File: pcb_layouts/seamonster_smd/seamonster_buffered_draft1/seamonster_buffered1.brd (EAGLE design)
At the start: 172.5 x 106.5 mm, 84 parts, among them IC1 7805T, IC2 4051D, IC3 4051D, IC4 DG408DY, IC5 4040D, IC6 40106D, IC7 4070D, Q1 THONKICONNNEW, Q2 THONKICONNNEW, Q3 THONKICONNNEW, Q4 THONKICONNNEW, Q5 THONKICONNNEW, Q6 THONKICONNNEW, SW1 T-80-T-SPDT-ON-OFF-ON, SW2 T-80-T-SPDT-ON-OFF-ON, SW3 T-80-T-SPDT-ON-OFF-ON, SW4 T-80-T-SPDT-ON-OFF-ON

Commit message: figured out invoking across multiple sheets
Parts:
- removed IC5: 4040D, 40xx:SO16
- removed LED10, LED11, LED12, LED13, LED14, LED9: (no value), SparkFun-LED:LED3MM
- removed Q1, Q2, Q3, Q4, Q5, Q6: THONKICONNNEW, MusicThingModular:WQP-PJ301M-12_JACK
- removed R10, R11, R12, R13, R14, R9: (no value), SparkFun-Resistors:0805
- added U1: TL084, MusicThingModular:SO14
- moved C5 521.2 mm to (-403.9, -256.5)
- moved C6 521.2 mm to (-407.7, -256.5)
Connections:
- removed net N$34: LED9.A, R9.1
- removed net N$35: LED10.A, R10.1
- removed net N$36: LED11.A, R11.1
- removed net N$37: LED12.A, R12.1
- removed net N$38: LED13.A, R13.1
- removed net N$39: LED14.A, R14.1
- removed net N$40: IC5.9, Q1.P$1_TIP, R9.2
- removed net N$41: IC5.7, Q2.P$1_TIP, R10.2
- removed net N$42: IC5.6, Q3.P$1_TIP
- removed net N$43: IC5.5, Q4.P$1_TIP
- removed net N$44: IC5.3, Q5.P$1_TIP
- removed net N$45: IC5.2, Q6.P$1_TIP
- removed net N$48: R11.2
- removed net N$49: R12.2
- removed net N$50: R13.2
- removed net N$51: R14.2
- new net CCO1_BUFFERED: U1.1, U1.2
- new net CCO2_BUFFERED: U1.6, U1.7
- new net CCO3_BUFFERED: U1.8, U1.9
- new net CCO4_BUFFERED: U1.13, U1.14
- new net VEE: IC2.7, IC3.7
- net CCO1: now also U1.3
- net GND: no longer IC2.7, IC3.7, LED10.K, LED11.K, LED12.K, LED13.K, LED14.K, LED9.K, Q1.P$3_SLEEVE, Q2.P$3_SLEEVE, Q3.P$3_SLEEVE, Q4.P$3_SLEEVE, Q5.P$3_SLEEVE, Q6.P$3_SLEEVE
- net N$54: now also U1.5
- net N$57: now also U1.10
- net N$61: now also U1.12
- net V+: now also C5.1, U1.4
- net V-: now also C6.1, U1.11
- net VCC: no longer C5.1, C6.1
- net VDD: no longer IC5.16
- net VSS: no longer IC5.8

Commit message: fleshed out schematic pages
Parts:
- added C15, C16, C17, C18, C19, C20: 0.1µF, SparkFun-Capacitors:0805
- added IC5, IC8: 4046D, 40xx:SO16
- added U2: TL084, MusicThingModular:SO14
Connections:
- removed net VEE: IC2.7, IC3.7
- new net COMPLEX_OUT1_BUFFERED: U2.1, U2.2
- new net COMPLEX_OUT2_BUFFERED: U2.6, U2.7
- new net N$34: IC7.1
- new net N$35: IC7.3, IC7.5
- new net N$36: IC7.10, IC7.12
- new net N$37: IC7.8
- new net N$38: IC7.4, U2.3
- new net N$39: IC7.11, U2.5
- net CCO1_BUFFERED: now also IC7.2
- net CCO2_BUFFERED: now also IC7.6
- net CCO3_BUFFERED: now also IC7.9
- net CCO4_BUFFERED: now also IC7.13
- net GND: now also C15.2, C16.2, C17.2, C18.2, C19.2, C20.2, IC2.7, IC3.7, IC6.7, IC7.7
- net V+: now also C18.1, U2.4
- net V-: now also C19.1, U2.11
- net VCC: now also C15.1, C16.1, C17.1, C20.1, IC6.14, IC7.14
- net VDD: now also IC5.16, IC8.16; no longer IC6.14, IC7.14
- net VSS: now also IC5.8, IC8.8; no longer IC6.7, IC7.7

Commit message: added in VCOs and more buffering
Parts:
- added C21, C22, C25, C26, C27, C28, C29: 0.1µF, SparkFun-Capacitors:0805
- added C23, C24: 1µF, SparkFun-Capacitors:0805
- added CLOCK_IN, CV_OUT, Q1, Q2, Q3, Q4, Q5, Q6: THONKICONNNEW, MusicThingModular:WQP-PJ301M-12_JACK
- added CLOCK_SELECT: T-80-T-SPDT-ON-OFF-ON, MusicThingModular:M9040P
- added IC9: 4040D, 40xx:SO16
- added LED10, LED11, LED12, LED13, LED14, LED9: (no value), SparkFun-LED:LED3MM
- added R10, R11, R12, R13, R14, R15, R16, R17, R18, R9: (no value), SparkFun-Resistors:0805
- added U3: TL084, MusicThingModular:SO14
- added VR13, VR14: 1MΩ, MusicThingModular:9MM_SNAP-IN_POT
- added VR15: 100KΩ, MusicThingModular:9MM_SNAP-IN_POT
- VR1, VR10, VR11, VR12, VR2, VR3, VR4, VR5, VR6, VR7, VR8: value (none) -> 100KΩ
- moved VR8 923.1 mm to (-468.6, -584.2), turned to 0 degrees
- moved VR7 886.7 mm to (-468.6, -552.5), turned to 0 degrees
- moved VR6 850.4 mm to (-468.6, -520.7), turned to 0 degrees
- moved VR5 814.1 mm to (-468.6, -488.9), turned to 0 degrees
- moved VR4 777.9 mm to (-468.6, -457.2), turned to 0 degrees
- moved VR3 741.8 mm to (-468.6, -425.4), turned to 0 degrees
- moved VR2 705.9 mm to (-468.6, -393.7), turned to 0 degrees
- moved VR10 699.2 mm to (-664.2, -793.8)
- moved VR11 699.2 mm to (-664.2, -825.5)
- moved VR12 699.2 mm to (-664.2, -857.2)
- moved VR9 699.2 mm to (-664.2, -762.0)
- moved VR1 670.0 mm to (-468.6, -361.9), turned to 0 degrees
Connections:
- removed net VDD: IC5.16, IC8.16
- removed net VSS: IC5.8, IC8.8
- new net CV_OUT_BUFFERED: CV_OUT.P$1_TIP, IC5.9, IC8.9, U2.8, U2.9
- new net N$40: IC5.12, R15.2
- new net N$41: IC6.1, VR15.1
- new net N$42: R15.1, VR13.3
- new net N$43: CLOCK_SELECT.3, IC6.2, VR15.2
- new net N$44: C23.1, IC5.6
- new net N$45: C23.2, IC5.7
- new net N$48: C24.1, IC8.6
- new net N$49: C24.2, IC8.7
- new net N$50: CLOCK_SELECT.2, IC9.10
- new net N$51: LED9.A, R9.2
- new net N$65: LED10.A, R10.2
- new net N$66: LED11.A, R11.2
- new net N$67: LED12.A, R12.2
- new net N$68: LED13.A, R13.2
- new net N$69: LED14.A, R14.2
- new net N$70: CLOCK_IN.P$1_TIP, CLOCK_SELECT.1
- new net N$71: IC8.12, R16.2
- new net N$72: R16.1, VR14.3
- new net N$74: IC8.11, R18.2
- new net N$75: IC5.11, R17.2
- new net Q1: IC9.9, Q1.P$1_TIP, R9.1
- new net Q2: IC9.7, Q2.P$1_TIP, R10.1
- new net Q3: IC9.6, Q3.P$1_TIP, R11.1
- new net Q4: IC9.5, Q4.P$1_TIP, R12.1
- new net Q5: IC9.3, Q5.P$1_TIP, R13.1
- new net Q6: IC9.2, Q6.P$1_TIP, R14.1
- new net VCO1_OUT: IC5.4, U3.3
- new net VCO1_OUT_BUFFERED: U3.1, U3.2
- new net VCO2_OUT: IC8.4, U3.5
- new net VCO2_OUT_BUFFERED: U3.6, U3.7
- net CV_OUT: now also U2.10
- net GND: now also C21.2, C22.2, C25.2, C26.2, C27.2, C28.2, C29.2, CLOCK_IN.P$3_SLEEVE, IC5.5, IC5.8, IC8.5, IC8.8, IC9.11, IC9.8, LED10.K, LED11.K, LED12.K, LED13.K, LED14.K, LED9.K, Q1.P$3_SLEEVE, Q2.P$3_SLEEVE, Q3.P$3_SLEEVE, Q4.P$3_SLEEVE, Q5.P$3_SLEEVE, Q6.P$3_SLEEVE, R17.1, R18.1, VR1.CHASSIS2, VR10.CHASSIS2, VR11.CHASSIS2, VR12.CHASSIS2, VR13.2, VR13.CHASSIS2, VR14.2, VR14.CHASSIS2, VR15.CHASSIS2, VR2.CHASSIS2, VR3.CHASSIS2, VR4.CHASSIS2, VR5.CHASSIS2, VR6.CHASSIS2, VR7.CHASSIS2, VR8.CHASSIS2, VR9.CHASSIS2
- net V+: now also C25.1, C28.1, U3.4
- net V-: now also C26.1, C29.1, U3.11
- net VCC: now also C21.1, C22.1, C27.1, IC4.2, IC5.16, IC8.16, IC9.16

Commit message: roughly positioned thruhole panel parts
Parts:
- added CCO1, CCO2, CCO3, CCO4, COMPLEX1, COMPLEX2, VCO1, VCO2: THONKICONNNEW, MusicThingModular:WQP-PJ301M-12_JACK
- CLOCK_SELECT, SW1, SW2, SW3, SW4: value T-80-T-SPDT-ON-OFF-ON -> SPDT ON-ON
- moved C28 1374.0 mm to (275.6, 95.2)
- moved R15 1374.0 mm to (290.8, 95.2)
- moved R17 1374.0 mm to (283.2, 95.2)
- moved C29 1374.0 mm to (271.8, 95.2)
- moved R16 1374.0 mm to (287.0, 95.2)
- moved R18 1374.0 mm to (279.4, 95.2)
- moved C27 1255.6 mm to (289.6, 50.8)
- moved VR12 1178.0 mm to (67.3, 66.0)
- moved VR11 1141.3 mm to (48.3, 66.0)
- moved VR10 1104.6 mm to (29.2, 66.0)
- moved LED14 1096.6 mm to (115.6, 29.2), turned to 180 degrees
- moved LED13 1090.7 mm to (125.7, 29.2), turned to 180 degrees
- moved LED12 1085.3 mm to (135.9, 29.2), turned to 180 degrees
- moved LED11 1080.3 mm to (146.1, 29.2), turned to 180 degrees
- moved LED10 1075.6 mm to (156.2, 29.2), turned to 180 degrees
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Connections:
- new net N$73: CCO1.P$3_SLEEVE, CCO2.P$3_SLEEVE, CCO3.P$3_SLEEVE, CCO4.P$3_SLEEVE, COMPLEX1.P$3_SLEEVE, COMPLEX2.P$3_SLEEVE
- net CCO1_BUFFERED: now also CCO1.P$1_TIP
- net CCO2_BUFFERED: now also CCO2.P$1_TIP
- net CCO3_BUFFERED: now also CCO3.P$1_TIP
- net CCO4_BUFFERED: now also CCO4.P$1_TIP
- net COMPLEX_OUT1_BUFFERED: now also COMPLEX1.P$1_TIP
- net COMPLEX_OUT2_BUFFERED: now also COMPLEX2.P$1_TIP
- net GND: now also CV_OUT.P$3_SLEEVE, VCO1.P$3_SLEEVE, VCO2.P$3_SLEEVE
- net VCO1_OUT_BUFFERED: now also VCO1.P$1_TIP
- net VCO2_OUT_BUFFERED: now also VCO2.P$1_TIP

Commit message: roughly placed all remaining parts
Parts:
- IC1: value 7805T -> 7808DT; device linear:TO220H -> linear:TO252
- moved C7 290.6 mm to (4.45, 56.5), turned to 180 degrees
- moved C8 275.4 mm to (15.9, 56.5), turned to 180 degrees
- moved C10 256.5 mm to (27.3, 56.5), turned to 180 degrees
- moved U1 253.7 mm to (21.6, 36.8)
- moved C9 249.0 mm to (38.7, 56.5), turned to 180 degrees
- moved C17 248.9 mm to (1.91, 36.8), turned to 270 degrees
- moved C5 245.6 mm to (21.6, 30.5), turned to 270 degrees
- moved R15 245.1 mm to (54.6, 29.8)
- moved C6 239.8 mm to (21.6, 43.2), turned to 90 degrees
- moved IC7 239.0 mm to (35.6, 36.8)
- moved C16 232.0 mm to (19.7, 87.0)
- moved C12 226.3 mm to (50.2, 56.5)
- moved R16 223.2 mm to (73.7, 29.8)
- moved C11 218.8 mm to (61.6, 56.5)
- moved C15 197.8 mm to (57.8, 87.0)
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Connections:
- net GND: now also IC1.3; no longer IC1.2
- net VCC: now also IC1.2; no longer IC1.3
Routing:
- net V-: track 0.00 -> 15.1 mm
- net V+: track 0.00 -> 14.8 mm

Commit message: added top and bottom layer ground pours, did basic layout
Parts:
- moved C14 1.27 mm to (73.0, 56.5)
- turned C10 to 0 degrees
- turned C11 to 180 degrees
- turned C13 to 180 degrees
- turned C7 to 0 degrees
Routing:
- net VCC: track 0.00 -> 167.6 mm
- net N$53: track 0.00 -> 50.6 mm
- net COMPLEX_OUT2_BUFFERED: track 0.00 -> 49.8 mm
- net COMPLEX_OUT1_BUFFERED: track 0.00 -> 49.4 mm
- net N$54: track 0.00 -> 48.2 mm
- net CCO1: track 0.00 -> 44.8 mm
- net N$46: track 0.00 -> 35.1 mm
- net N$57: track 0.00 -> 19.4 mm
- net N$58: track 0.00 -> 10.6 mm
- net N$62: track 0.00 -> 10.5 mm
- net N$17: track 0.00 -> 9.94 mm
- net V-: track 15.1 -> 23.3 mm
- net V+: track 14.8 -> 23.0 mm
- net N$64: track 0.00 -> 6.51 mm
- net N$55: track 0.00 -> 6.51 mm
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- added copper zone on layer 1, net GND
- added copper zone on layer 16, net GND

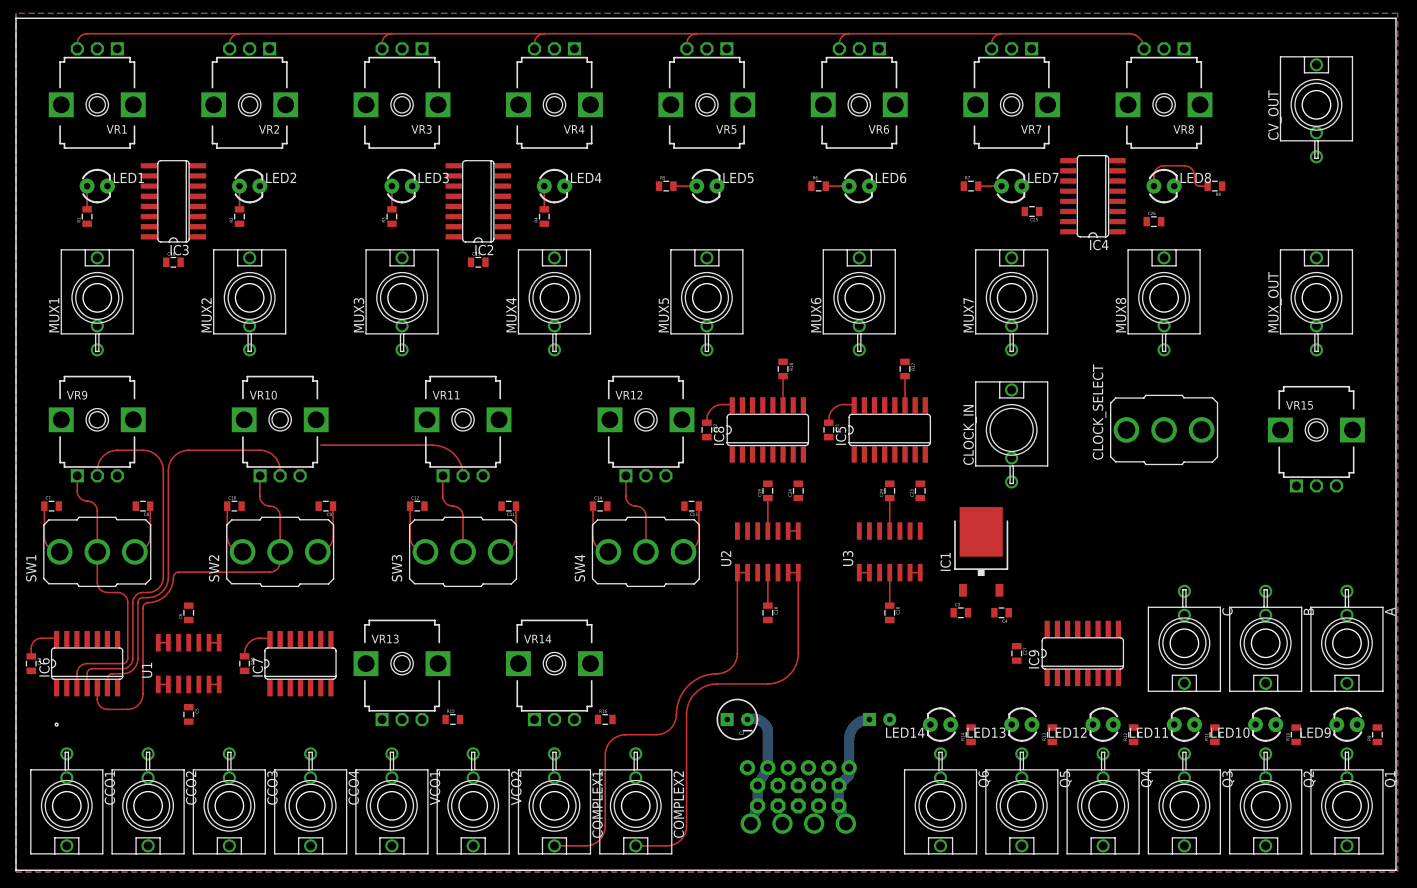
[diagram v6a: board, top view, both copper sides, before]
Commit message: routed ABC bus between 4051s, more basic routing
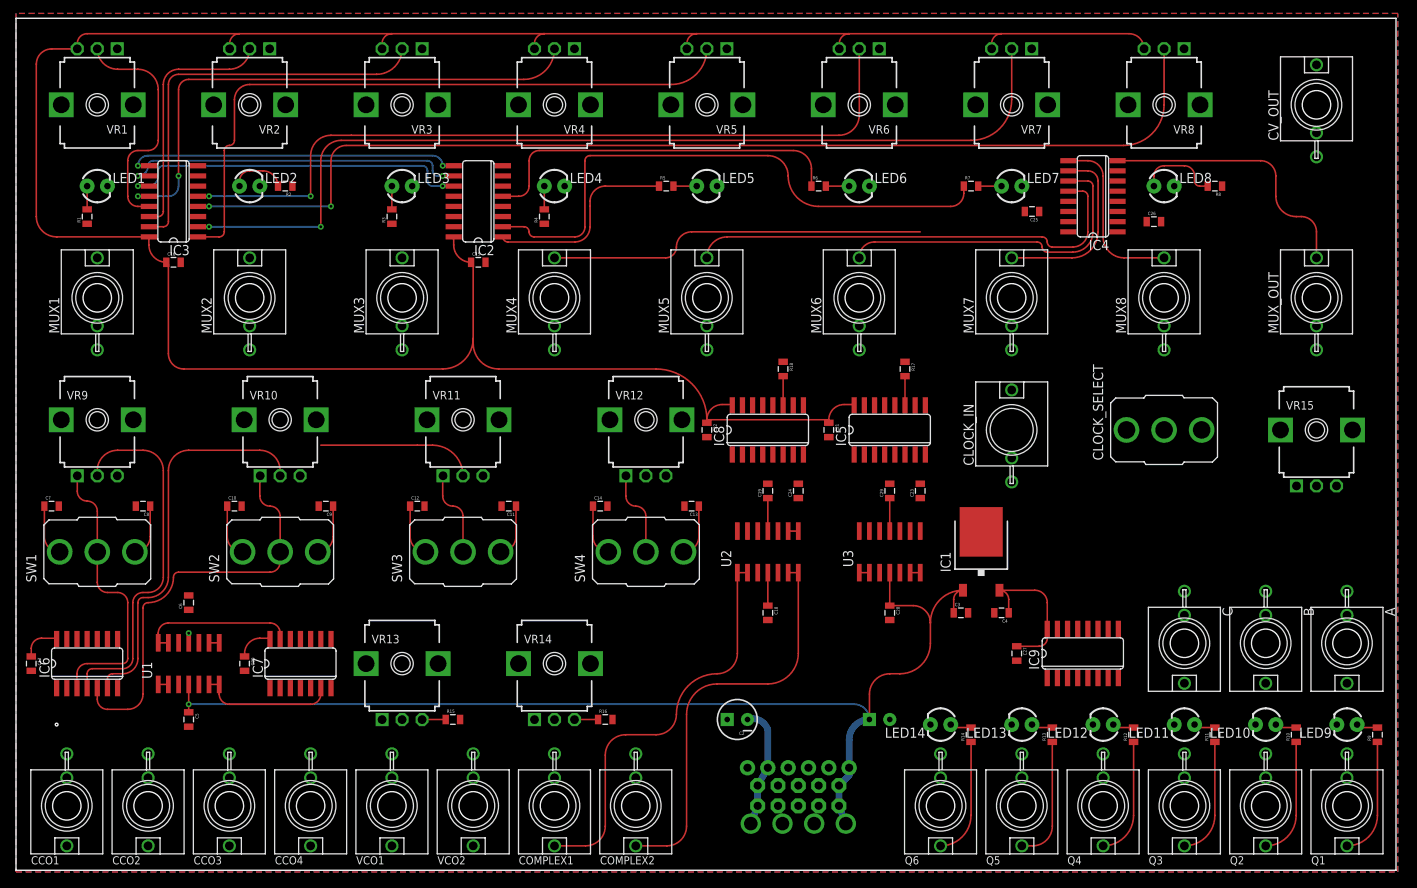
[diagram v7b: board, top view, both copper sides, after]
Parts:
- moved R2 6.87 mm to (33.7, 96.5), turned to 180 degrees
- moved C6 1.27 mm to (21.6, 44.5)
- moved C5 0.64 mm to (21.6, 29.8)
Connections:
- removed net N$34: IC7.1
- removed net N$37: IC7.8
- net VCO2_OUT_BUFFERED: now also IC7.1, IC7.8
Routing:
- net VCC: track 167.6 -> 345.1 mm
- net N$33: track 0.00 -> 136.4 mm, vias 0 -> 2
- net V+: track 23.0 -> 143.4 mm, vias 0 -> 1
- net N$32: track 0.00 -> 119.5 mm, vias 0 -> 2
- net N$31: track 0.00 -> 98.1 mm, vias 0 -> 2
- net N$30: track 0.00 -> 82.3 mm
- net N$25: track 0.00 -> 71.4 mm
- net N$29: track 0.00 -> 68.1 mm, vias 0 -> 2
- net N$6: track 0.00 -> 57.2 mm
- net N$28: track 0.00 -> 50.9 mm
- net N$5: track 0.00 -> 47.1 mm
- net N$24: track 0.00 -> 45.9 mm
- net A: track 0.00 -> 44.1 mm, vias 0 -> 2
- net B: track 0.00 -> 42.8 mm, vias 0 -> 2
- net C: track 0.00 -> 41.8 mm, vias 0 -> 2
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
